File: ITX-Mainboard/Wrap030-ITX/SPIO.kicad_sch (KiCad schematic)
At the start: 0 parts

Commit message: Schematic substantial completion
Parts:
- added C1, C13, C14, C3, C4: 100nF, Capacitor_SMD:C_0402_1005Metric_Pad0.74x0.62mm_HandSolder, symbol Device:C_Small
- added C15 (x9): 1uF, Capacitor_SMD:C_0402_1005Metric_Pad0.74x0.62mm_HandSolder, symbol Device:C_Small
- added C3 (x8): 2200pF, Capacitor_SMD:C_0402_1005Metric_Pad0.74x0.62mm_HandSolder, symbol Device:C_Small
- added J11, J12: DE9_Plug_MountingHoles, Wrap030-ITX:DE9, symbol Connector:DE9_Plug_MountingHoles
- added J2: Conn_01x03, Connector_PinHeader_2.54mm:PinHeader_1x03_P2.54mm_Vertical, symbol Connector_Generic:Conn_01x03
- added PAR0: DB25_Receptacle_MountingHoles, Wrap030-ITX:DB25, symbol Connector:DB25_Receptacle_MountingHoles
- added U19: 74LS139, Package_DIP:DIP-16_W7.62mm_Socket, symbol 74xx:74LS139
- added U20: WD16C552, Package_LCC:PLCC-68_THT-Socket, symbol Wrap030-ITX:WD16C552
- added U21, U22: MAX232, Package_DIP:DIP-16_W7.62mm_Socket, symbol Interface_UART:MAX232
- added X2: 1.6862M, Oscillator:Oscillator_DIP-8, symbol Oscillator:CXO_DIP8
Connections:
- new net COM0-C1M: C15.2, U21.3 (C1-)
- new net COM0-C1P: C15.1, U21.1 (C1+)
- new net COM0-C2M: C15.1, U21.5 (C2-)
- new net COM0-C2P: C15.2, U21.4 (C2+)
- new net COM0-CTS232: J11.8, U21.8 (R2IN)
- new net COM0-RTS232: J11.7, U21.7 (T2OUT)
- new net COM0-RX232: J11.2, U21.13 (R1IN)
- new net COM0-SIN: U20.41 (SIN0), U21.12 (R1OUT)
- new net COM0-SOUT: U20.26 (SOUT0), U21.11 (T1IN)
- new net COM0-TX232: J11.3, U21.14 (T1OUT)
- new net COM0-VM: C15.1, U21.6 (VS-)
- new net COM0-VP: C15.1, U21.2 (VS+)
- new net COM1-C1M: C15.2, U22.3 (C1-)
- new net COM1-C1P: C15.1, U22.1 (C1+)
- new net COM1-C2M: C15.1, U22.5 (C2-)
- new net COM1-C2P: C15.2, U22.4 (C2+)
- new net COM1-CTS232: J12.8, U22.8 (R2IN)
- new net COM1-RTS232: J12.7, U22.7 (T2OUT)
- new net COM1-RX232: J12.2, U22.13 (R1IN)
- new net COM1-SIN: U20.62 (SIN1), U22.12 (R1OUT)
- new net COM1-SOUT: U20.10 (SOUT1), U22.11 (T1IN)
- new net COM1-TX232: J12.3, U22.14 (T1OUT)
- new net COM1-VM: C15.1, U22.6 (VS-)
- new net COM1-VP: C15.1, U22.2 (VS+)
- new net CPU-A3: U20.35 (A0)
- new net CPU-A4: U20.34 (A1)
- new net CPU-A5: U20.33 (A2)
- new net CPU-A6: U19.13 (A1)
- new net CPU-A7: U19.14 (A0)
- new net CPU-D24: U20.14 (D0)
- new net CPU-D25: U20.15 (D1)
- new net CPU-D26: U20.16 (D2)
- new net CPU-D27: U20.17 (D3)
- new net CPU-D28: U20.18 (D4)
- new net CPU-D29: U20.19 (D5)
- new net CPU-D30: U20.20 (D6)
- new net CPU-D31: U20.21 (D7)
- new net GND: C1.2, C13.2, C14.2, C15.2, C15.2, C15.2, C3.2, C4.2, J11.5, J12.5, J2.3 (Pin_3), PAR0.18 (P18), PAR0.19 (P19), PAR0.20 (P20), PAR0.21 (P21), PAR0.22 (P22), PAR0.23 (P23), PAR0.24 (P24), PAR0.25 (P25), U20.2 (GND), U20.43 (GND), U20.54 (GND), U20.7 (GND), U21.15 (GND), U22.15 (GND), X2.4 (GND)
- new net PAR-BIDEN: J2.2 (Pin_2), U20.1 (BIDEN)
- new net PAR-BUSY: PAR0.11, U20.66 (BUSY)
- new net PAR-D0: C3.1, U20.53 (PD0)
- new net PAR-D0-C: C3.2, PAR0.2
- new net PAR-D1: C3.1, U20.52 (PD1)
- new net PAR-D1-C: C3.2, PAR0.3
- new net PAR-D2: C3.1, U20.51 (PD2)
- new net PAR-D2-C: C3.2, PAR0.4
- new net PAR-D3: C3.1, U20.50 (PD3)
- new net PAR-D3-C: C3.2, PAR0.5
- new net PAR-D4: C3.1, U20.49 (PD4)
- new net PAR-D4-C: C3.2, PAR0.6
- new net PAR-D5: C3.1, U20.48 (PD5)
- new net PAR-D5-C: C3.2, PAR0.7
- new net PAR-D6: C3.1, U20.47 (PD6)
- new net PAR-D6-C: C3.2, PAR0.8
- new net PAR-D7: C3.1, U20.46 (PD7)
- new net PAR-D7-C: C3.2, PAR0.9
- new net PAR-PE: PAR0.12, U20.67 (PE)
- new net PAR-SLCT: PAR0.13, U20.65 (SLCT)
- new net SPIO-CLK: U20.4 (COM-CLK), X2.5 (OUT)
- new net VCC: C1.1, C13.1, C14.1, C15.1, C15.2, C15.2, C3.1, C4.1, J2.1 (Pin_1), U20.23 (VCC), U20.27 (VCC), U20.40 (VCC), U20.64 (VCC), U21.16 (VCC), U22.16 (VCC), X2.8 (Vcc)
- new net ~{COM0-CTS}: U20.28 (~{CTS0}), U21.9 (R2OUT)
- new net ~{COM0-RTS}: U20.24 (~{RTS0}), U21.10 (T2IN)
- new net ~{COM1-CTS}: U20.13 (~{CTS1}), U22.9 (R2OUT)
- new net ~{COM1-RTS}: U20.12 (~{RTS1}), U22.10 (T2IN)
- new net ~{MEM-RD}: U20.37 (~{IOR})
- new net ~{MEM-WR}: U20.36 (~{IOW})
- new net ~{PAR-ACK}: PAR0.10, U20.68 (~{ACK})
- new net ~{PAR-AFD}: PAR0.14 (P14), U20.56 (~{AFD})
- new net ~{PAR-ERR}: PAR0.15 (P15), U20.63 (~{ERR})
- new net ~{PAR-INIT}: PAR0.16 (P16), U20.57 (~{INIT})
- new net ~{PAR-SLIN}: PAR0.17 (P17), U20.58 (~{SLIN})
- new net ~{PAR-STB}: PAR0.1, U20.55 (~{STB})
- new net ~{RESET}: U20.39 (~{MR})
- new net ~{SPIO-CE}: U19.15 (E)
- new net ~{SPIO-CS0}: U19.12 (O0), U20.32 (~{CS0})
- new net ~{SPIO-CS1}: U19.11 (O1), U20.3 (~{CS1})
- new net ~{SPIO-CS2}: U19.10 (O2), U20.38 (~{CS2})
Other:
- company: (none) -> techav
- title: (none) -> Wrap030 ITX

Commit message: PCB substantial completion
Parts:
- removed J11, J12: DE9_Plug_MountingHoles, Wrap030-ITX:DE9, symbol Connector:DE9_Plug_MountingHoles
- removed PAR0: DB25_Receptacle_MountingHoles, Wrap030-ITX:DB25, symbol Connector:DB25_Receptacle_MountingHoles
- added J14: L17H26R0121, Wrap030-ITX:L17H26R0121, symbol Wrap030-ITX:L17H26R0121
- added unit 1 of U19
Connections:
- net COM0-CTS232: now also J14.A8
- net COM0-RTS232: now also J14.A7
- net COM0-RX232: now also J14.A2
- net COM0-TX232: now also J14.A3
- net COM1-CTS232: now also J14.B8
- net COM1-RTS232: now also J14.B7
- net COM1-RX232: now also J14.B2
- net COM1-TX232: now also J14.B3
- net GND: now also J14.0, J14.0, J14.0, J14.A5, J14.B5, J14.C18, J14.C19, J14.C20, J14.C21, J14.C22, J14.C23, J14.C24, J14.C25, U19.2 (A0), U19.3 (A1)
- net PAR-BUSY: now also J14.C11
- net PAR-D0-C: now also J14.C2
- net PAR-D1-C: now also J14.C3
- net PAR-D2-C: now also J14.C4
- net PAR-D3-C: now also J14.C5
- net PAR-D4-C: now also J14.C6
- net PAR-D5-C: now also J14.C7
- net PAR-D6-C: now also J14.C8
- net PAR-D7-C: now also J14.C9
- net PAR-PE: now also J14.C12
- net PAR-SLCT: now also J14.C13
- net VCC: now also U19.1 (E)
- net ~{PAR-ACK}: now also J14.C10
- net ~{PAR-AFD}: now also J14.C14
- net ~{PAR-ERR}: now also J14.C15
- net ~{PAR-INIT}: now also J14.C16
- net ~{PAR-SLIN}: now also J14.C17
- net ~{PAR-STB}: now also J14.C1
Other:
- moved on the sheet: C3

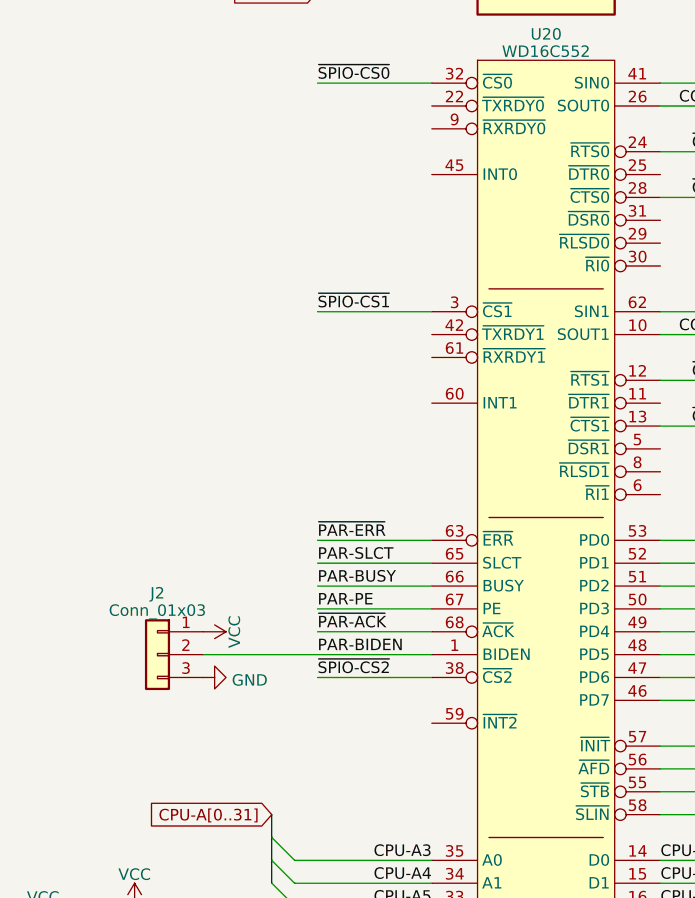
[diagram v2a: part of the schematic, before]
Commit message: Add interrupt controller to schematic
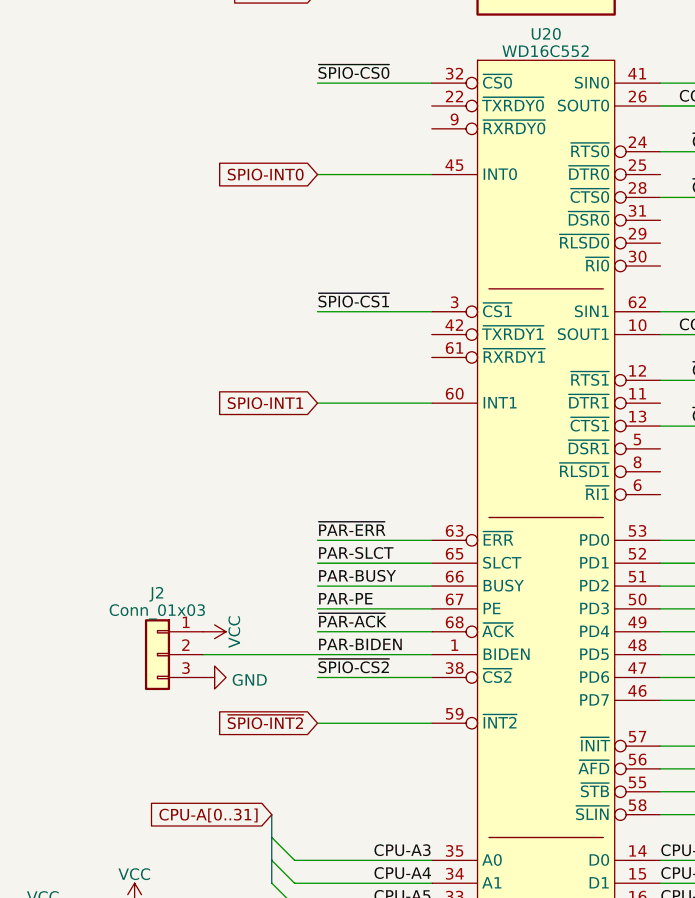
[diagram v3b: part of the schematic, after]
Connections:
- net SPIO-INT0: now reaches U20.45 (INT0)
- net ~{SPIO-INT2}: now reaches U20.59 (~{INT2})
- net SPIO-INT1: now reaches U20.60 (INT1)
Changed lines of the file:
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@@
+    (stroke (width 0) (type default))
+  )
+  (wire (pts (xy 45.72 50.8) (xy 58.42 50.8))
     (stroke (width 0) (type default))
   )
@@
     (stroke (width 0) (type default))
   )
+  (wire (pts (xy 45.72 76.2) (xy 58.42 76.2))
+    (stroke (width 0) (type default))
+  )
   (wire (pts (xy 71.12 165.1) (xy 71.12 167.64))
     (stroke (width 0) (type default))
@@
     (stroke (width 0) (type default))
   )
+  (wire (pts (xy 45.72 111.76) (xy 58.42 111.76))
+    (stroke (width 0) (type default))
+  )
   (wire (pts (xy 83.82 25.4) (xy 96.52 25.4))
     (stroke (width 0) (type default))
@@
   (label "~{COM1-CTS}" (at 119.38 137.16 0) (fields_autoplaced)
     (effects (font (size 1.27 1.27)) (justify left bottom))
+  )
+  (global_label "SPIO-INT1" (shape input) (at 45.72 76.2 180) (fields_autoplaced)
+    (effects (font (size 1.27 1.27)) (justify right))
+    (property "Intersheetrefs" "${INTERSHEET_REFS}" (at 32.7146 76.2 0)
+      (effects (font (size 1.27 1.27)) (justify right) hide)
+    )
   )
   (global_label "~{RESET}" (shape input) (at 45.72 142.24 180) (fields_autoplaced)
@@
       (effects (font (size 1.27 1.27)) (justify right) hide)
     )
+  )
+  (global_label "~{SPIO-INT2}" (shape input) (at 45.72 111.76 180) (fields_autoplaced)
+    (effects (font (size 1.27 1.27)) (justify right))
+    (property "Intersheetrefs" "${INTERSHEET_REFS}" (at 32.7146 111.76 0)
+      (effects (font (size 1.27 1.27)) (justify right) hide)
+    )
+  )
+  (global_label "SPIO-INT0" (shape input) (at 45.72 50.8 180) (fields_autoplaced)
+    (effects (font (size 1.27 1.27)) (justify right))
+    (property "Intersheetrefs" "${INTERSHEET_REFS}" (at 32.7146 50.8 0)
+      (effects (font (size 1.27 1.27)) (justify right) hide)
+    )

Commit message: Completing PCB Routing
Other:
- title: Wrap030 ITX -> Wrap030-ATX Mainboard
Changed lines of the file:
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@@
   (paper "USLetter")
   (title_block
-    (title "Wrap030 ITX")
-    (date "2023-03-15")
-    (rev "0")
+    (title "Wrap030-ATX Mainboard")
+    (date "2023-03-26")
+    (rev "1")
     (company "techav")
   )

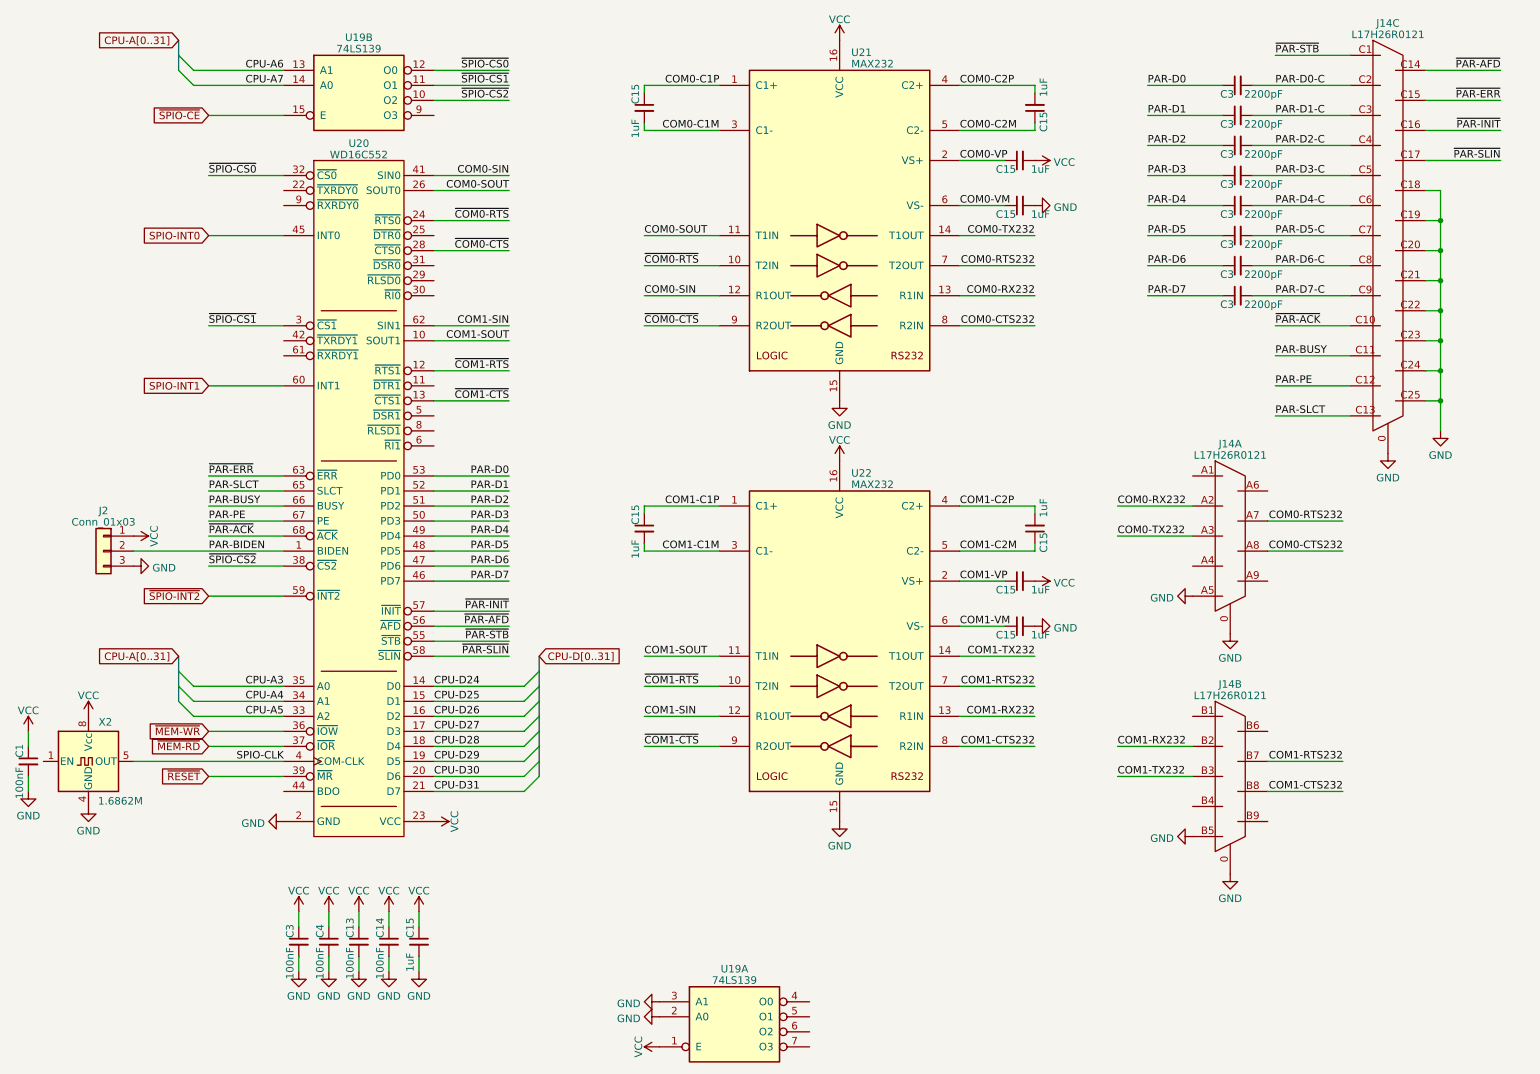
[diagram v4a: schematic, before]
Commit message: PCB Silkscreen & DRC Cleanup
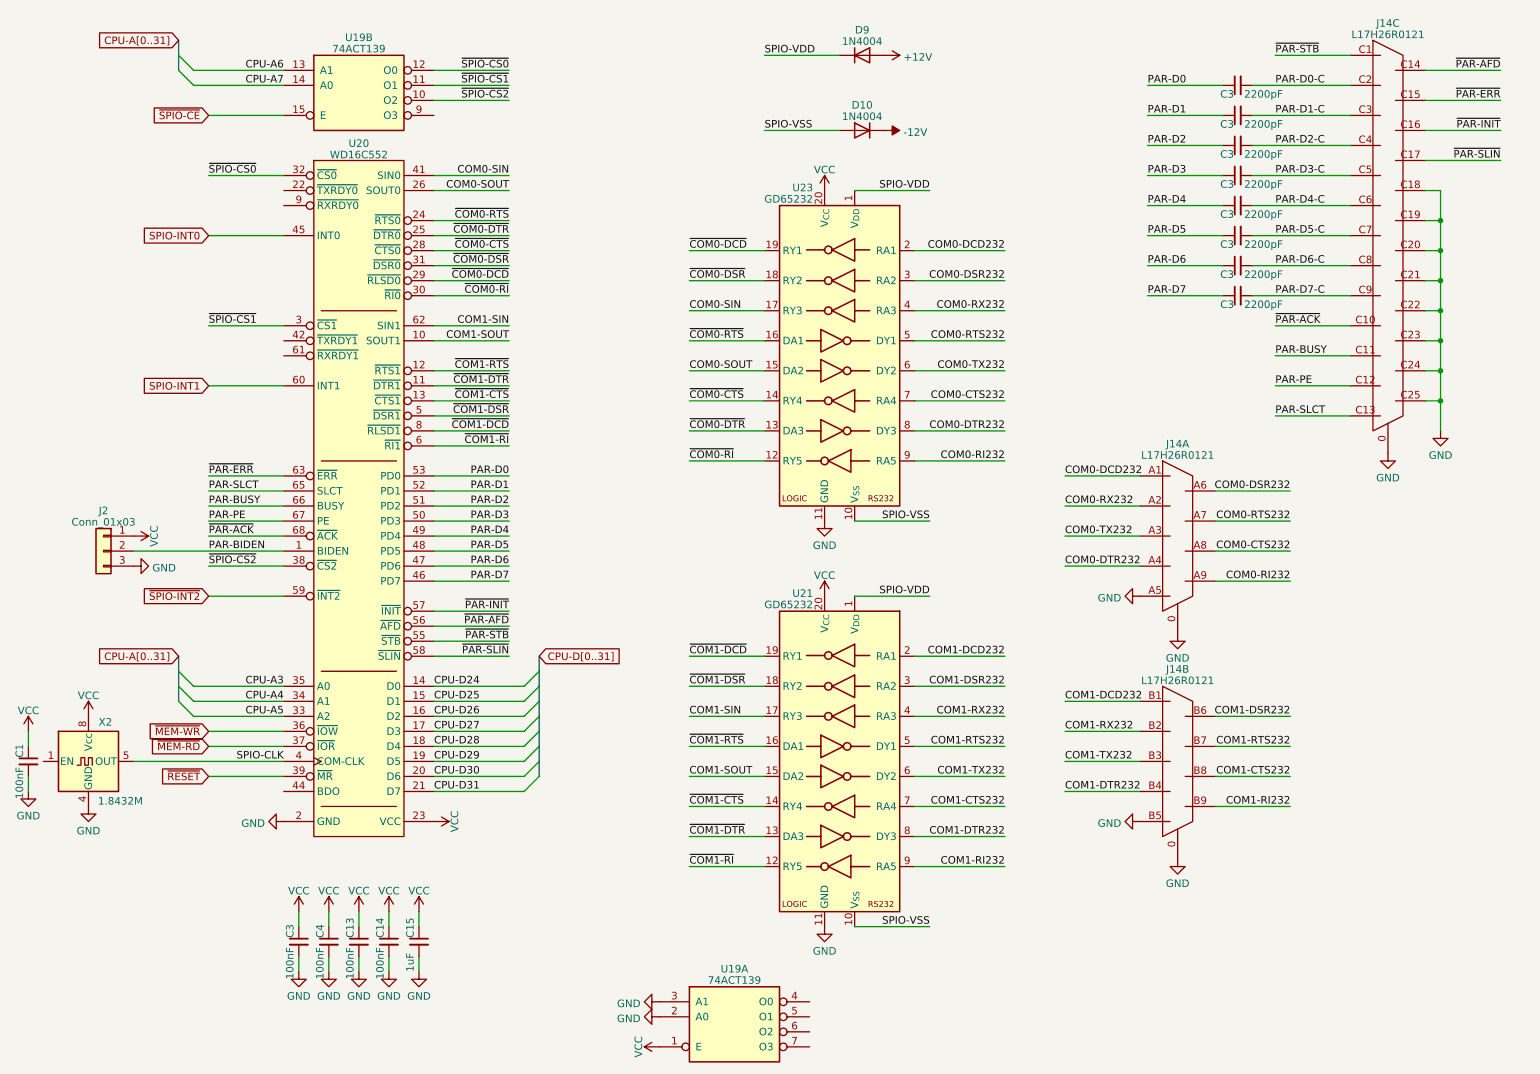
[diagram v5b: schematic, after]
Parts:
- removed C15 (x8): 1uF, Capacitor_SMD:C_0402_1005Metric_Pad0.74x0.62mm_HandSolder, symbol Device:C_Small
- removed U21, U22: MAX232, Package_DIP:DIP-16_W7.62mm_Socket, symbol Interface_UART:MAX232
- added D10, D9: 1N4004, Diode_THT:D_DO-41_SOD81_P10.16mm_Horizontal, symbol Diode:1N4004
- added U21, U23: GD65232, Package_SO:TSSOP-20_4.4x6.5mm_P0.65mm, symbol Interface_UART:GD65232PW
- U19: value 74LS139 -> 74ACT139
- X2: value 1.6862M -> 1.8432M
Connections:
- net COM0-CTS232: now also U23.7 (RA4)
- net COM0-RTS232: now also U23.5 (DY1)
- net COM0-RX232: now also U23.4 (RA3)
- net COM0-SIN: now also U23.17 (RY3)
- net COM0-SOUT: now also U23.15 (DA2)
- net COM0-TX232: now also U23.6 (DY2)
- net COM1-CTS232: now also U21.7 (RA4)
- net COM1-RTS232: now also U21.5 (DY1)
- net COM1-RX232: now also U21.4 (RA3)
- net COM1-SIN: now also U21.17 (RY3)
- net COM1-SOUT: now also U21.15 (DA2)
- net COM1-TX232: now also U21.6 (DY2)
- net GND: now also U21.11 (GND), U23.11 (GND)
- net VCC: now also U21.20 (V_{CC}), U23.20 (V_{CC})
- net ~{COM0-CTS}: now also U23.14 (RY4)
- net ~{COM0-RTS}: now also U23.16 (DA1)
- net ~{COM1-CTS}: now also U21.14 (RY4)
- net ~{COM1-RTS}: now also U21.16 (DA1)
- net ~{COM1-DTR}: now reaches U20.11 (~{DTR1})
- net ~{COM1-DTR}: now also U21.13 (DA3)
- net ~{COM0-DTR}: now reaches U20.25 (~{DTR0})
- net ~{COM0-DTR}: now also U23.13 (DA3)
- net ~{COM0-DCD}: now reaches U20.29 (~{RLSD0})
- net ~{COM0-DCD}: now also U23.19 (RY1)
- net ~{COM0-RI}: now reaches U20.30 (~{RI0})
- net ~{COM0-RI}: now also U23.12 (RY5)
- net ~{COM0-DSR}: now reaches U20.31 (~{DSR0})
- net ~{COM0-DSR}: now also U23.18 (RY2)
- net ~{COM1-DSR}: now reaches U20.5 (~{DSR1})
- net ~{COM1-DSR}: now also U21.18 (RY2)
- net ~{COM1-RI}: now reaches U20.6 (~{RI1})
- net ~{COM1-RI}: now also U21.12 (RY5)
- net ~{COM1-DCD}: now reaches U20.8 (~{RLSD1})
- net ~{COM1-DCD}: now also U21.19 (RY1)
- net COM0-DCD232: now reaches J14.A1
- net COM0-DCD232: now also U23.2 (RA1)
- net COM0-DTR232: now reaches J14.A4
- net COM0-DTR232: now also U23.8 (DY3)
- net COM0-DSR232: now reaches J14.A6
- net COM0-DSR232: now also U23.3 (RA2)
- net COM0-RI232: now reaches J14.A9
- net COM0-RI232: now also U23.9 (RA5)
- net COM1-DCD232: now reaches J14.B1
- net COM1-DCD232: now also U21.2 (RA1)
- net COM1-DTR232: now reaches J14.B4
- net COM1-DTR232: now also U21.8 (DY3)
- net COM1-DSR232: now reaches J14.B6
- net COM1-DSR232: now also U21.3 (RA2)
- net COM1-RI232: now reaches J14.B9
- net COM1-RI232: now also U21.9 (RA5)
- new net +12V: D9.2 (A)
- new net -12V: D10.1 (K)
- new net SPIO-VDD: D9.1 (K), U21.1 (V_{DD}), U23.1 (V_{DD})
- new net SPIO-VSS: D10.2 (A), U21.10 (V_{SS}), U23.10 (V_{SS})
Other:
- moved on the sheet: J14A, J14B

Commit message: initial production schematic
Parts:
- J2: value Conn_01x03 -> BIDEN
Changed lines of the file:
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@@
       (effects (font (size 1.27 1.27)))
     )
-    (property "Value" "Conn_01x03" (at 27.94 99.2411 0)
+    (property "Value" "BIDEN" (at 27.94 99.2411 0)
       (effects (font (size 1.27 1.27)))
     )

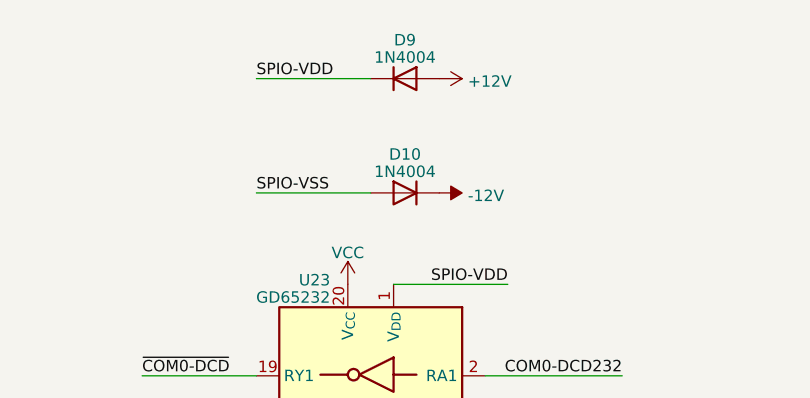
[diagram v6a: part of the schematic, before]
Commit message: Replace resistor nets with 0402 & update gerbers
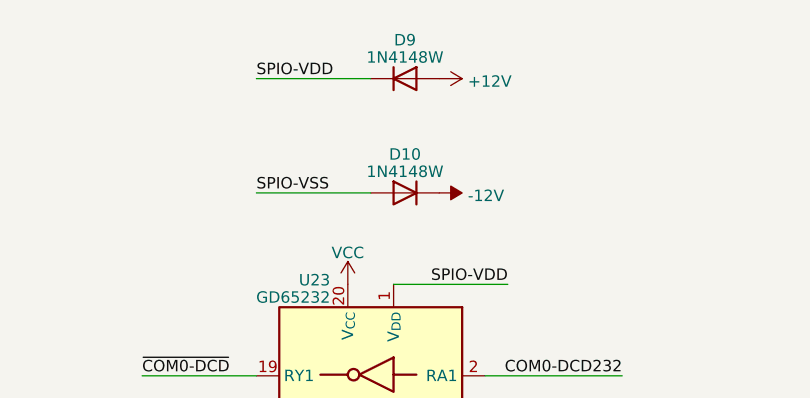
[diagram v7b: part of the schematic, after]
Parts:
- C1, C13, C14, C3, C4: Mouser-Part (none) -> 187-CL05B104KO5NNNC; Notes (none) -> JLC
- C15: Mouser-Part (none) -> 187-CL05A105KA5NQNC; Notes (none) -> JLC
- C3: Mouser-Part (none) -> 81-GRM155R71H222KA1J; Notes (none) -> JLC
- D10, D9: value 1N4004 -> 1N4148W; footprint Diode_THT:D_DO-41_SOD81_P10.16mm_Horizontal -> Diode_SMD:D_SOD-123; JLC-Part (none) -> https://jlcpcb.com/partdetail/st_semtech-1N4148W/C81598; Mouser-Part (none) -> 833-1N4148W-TP; Notes (none) -> JLC
- J14: Mouser-Part (none) -> 523-L17H26R0121; Notes (none) -> Mouser
- J2: Mouser-Part (none) -> 523-G800W305018EU; Notes (none) -> OFE
- U19: Mouser-Part (none) -> 595-CD74ACT139E; Notes (none) -> OFE; Socket-Mouser (none) -> 571-1-2199298-4
- U20: Mouser-Part (none) -> 595-TL16C552AIFN; Notes (none) -> OFE; Socket-Mouser (none) -> 575-682444
- U21, U23: Mouser-Part (none) -> 595-GD65232PWR; Notes (none) -> Mouser
- X2: Mouser-Part (none) -> 520-TCH184-X; Notes (none) -> Mouser
